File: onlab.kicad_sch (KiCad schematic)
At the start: 82 parts, among them J1 Battery, J10 DC-Motor, J2 HC_SR04, J3 HC_SR04, J4 HC_SR04, J5 DC-Motor, J6 DC-Motor, J7 DC-Motor, J8 DC-Motor, J9 DC-Motor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

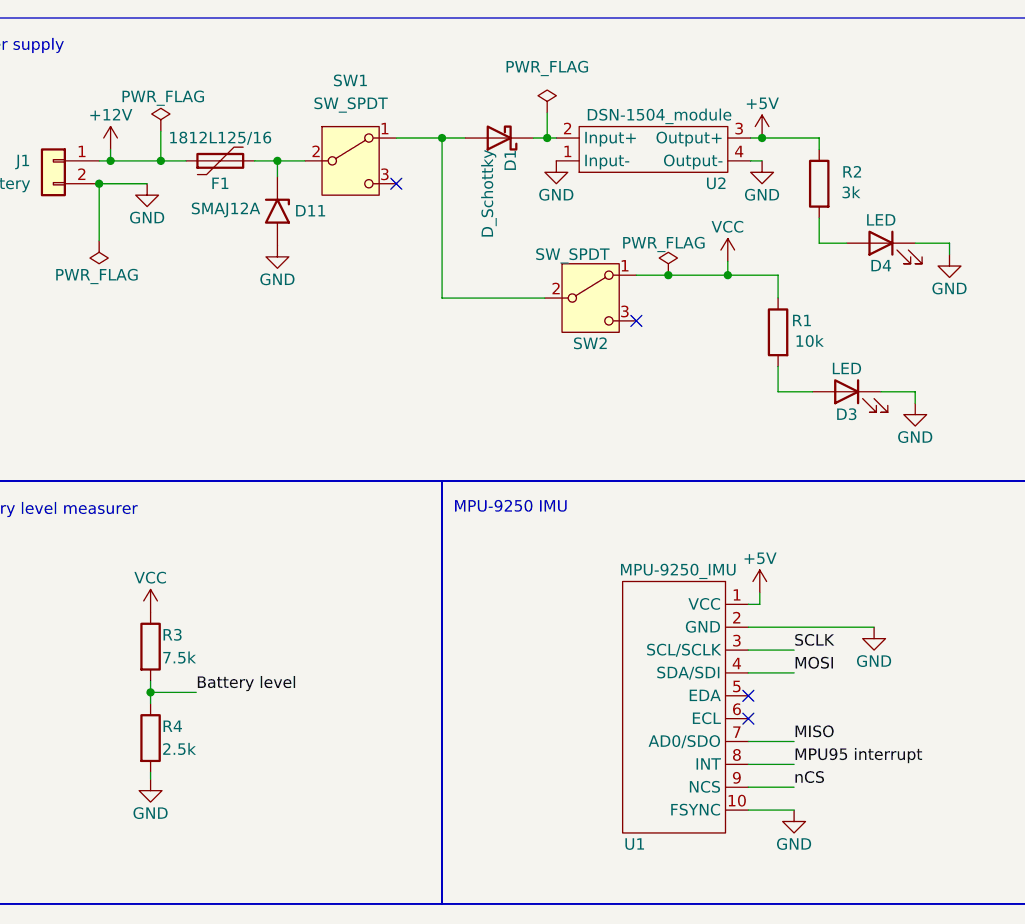
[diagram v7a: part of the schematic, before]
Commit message: resistor value update 2
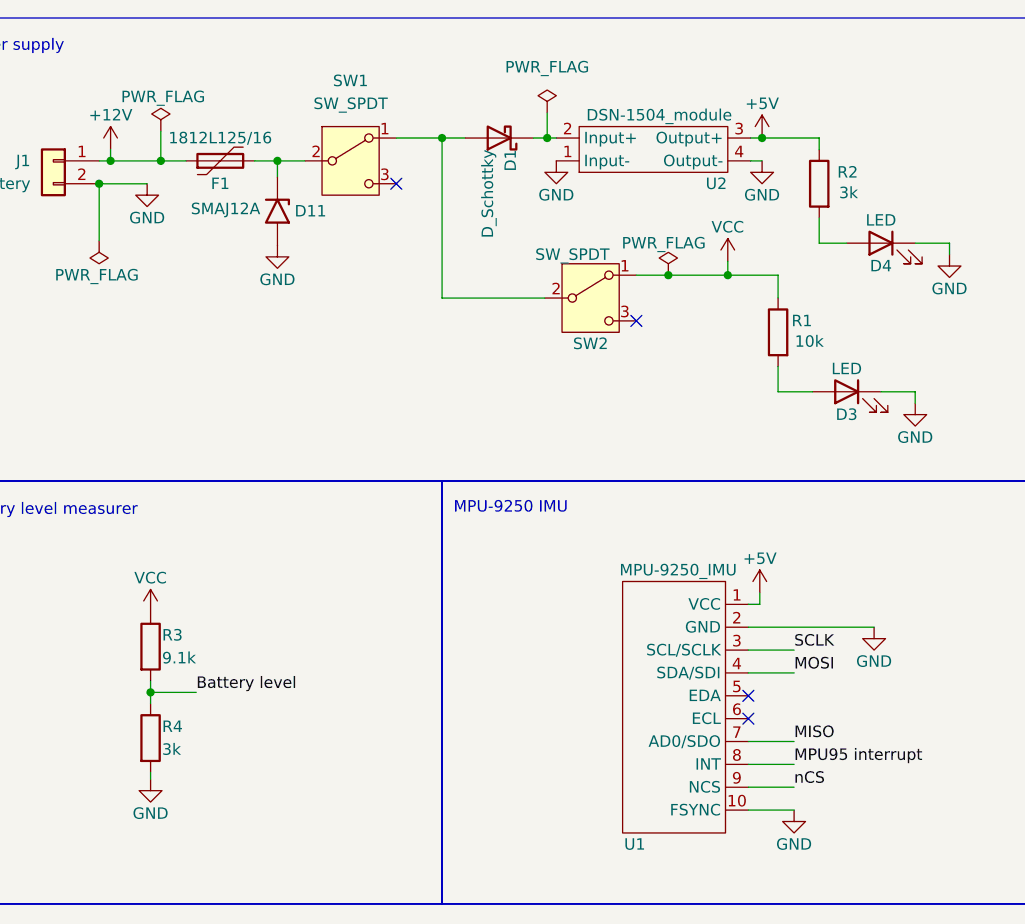
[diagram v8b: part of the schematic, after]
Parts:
- R3: value 7.5k -> 9.1k
- R4: value 2.5k -> 3k
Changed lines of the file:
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@@
 		(dnp no)
 		(property "Reference" "R2"
-			(at 114.046 29.21 0)
+			(at 113.538 29.21 0)
 			(effects
 				(font
@@
 		)
 		(property "Value" "3k"
-			(at 113.792 31.496 0)
+			(at 113.538 31.496 0)
 			(effects
 				(font
@@
 			)
 		)
-		(property "Value" "7.5k"
+		(property "Value" "9.1k"
 			(at 36.195 83.185 0)
 			(effects
@@
 			)
 		)
-		(property "Value" "2.5k"
+		(property "Value" "3k"
 			(at 36.195 93.345 0)
 			(effects
